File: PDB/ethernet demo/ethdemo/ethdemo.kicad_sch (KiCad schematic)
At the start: 102 parts, among them J1 0826-1X1T-GJ-F, J2 0826-1X1T-GJ-F, Q1 CSD19538Q3AT, U1 STM32H742VGTx, U2 KSZ8863RLLI, U3 TPS23861PWR, Y1 25MHz

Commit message: finished PoE schem start demo layout
started layout and fixed crystal footprint, still need to do I2C on MCU and RMII, need confirmation that MCU labels are old and can be overwritten
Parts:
- added R32: 10kOhm, Resistor_SMD:R_0603_1608Metric, symbol Device:R
- C24, C25: value 5pF -> 10pF
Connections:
- net +3.3V: now also C10.1, R47.2, U3.1 (VDD), U3.2 (~{RESET}), U3.24 (~{SHTDWN}), R32.2; no longer R48.2
- net Clock: now also U3.3 (SCL); no longer R31.2, U2.36 (SCL_MDC)
- net Data: now also U3.4 (SDAI), U3.5 (SDAO), R32.1
- net GND: now also R48.2; no longer R47.2, U3.23 (A3), U3.3 (SCL), U3.4 (SDAI)
- net P1LED0: no longer J1.19, R47.1
- net P1LED1: no longer J1.17, R48.1
- net P2LED0: now also J1.19, R47.1
- net P2LED1: now also J1.17, R48.1
- net Lost Connect: now reaches R30.1
- new net Address: U3.23 (A3)
- new net Cock: R31.2, U2.36 (SCL_MDC)
- no-connect marks 64 -> 63
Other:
- moved on the sheet: C10, C11, C12, C15, C16, C17, C18, C19, C20, C21, C22, C23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

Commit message: Finished first draft of demo schem
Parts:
- removed D1, D2: LED, LED_SMD:LED_0805_2012Metric, symbol Device:LED
- removed D6: 60V, symbol Device:D_Zener
- removed D7: 100V, symbol Device:D_Zener
- removed R1, R2: 270, Resistor_SMD:R_0603_1608Metric, symbol Device:R
- added D6: SMCJ60A, foot:SMCJ60A, symbol sym&foot:SMCJ60A
- added D7: SMAJ4764A-TP, foot:SMAJ100CA_13_F, symbol sym&foot:SMAJ4764A-TP
- C12, C15, C16, C17, C18, C19, C20, C21, C22, C23, C24, C25, C26, C27, C28, C29, C30, C31, C32, C33, C34, C35, C36: footprint (none) -> Capacitor_SMD:C_0603_1608Metric
- J1, J2: footprint 0826-1X1T-GJ-F:BEL_0826-1X1T-GJ-F -> foot:0826-1X1T-GJ-F
- R12, R13, R14, R15, R16, R17, R18, R19, R20, R21, R22, R23, R24, R25, R26, R27, R28, R29, R30, R31, R34, R35, R36, R37, R38, R39, R40, R41, R42, R43, R44, R45, R46, R47, R48, R49, R50: footprint (none) -> Resistor_SMD:R_0603_1608Metric
- U2: footprint LQFP-48_MCL -> foot:KSZ8863RLLI
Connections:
- net Cock is gone; now on net Clock: R31.2, U2.36 (SCL_MDC)
- net MOSI is gone; now on net CRS_DV: U1.31 (PA7)
- net PB11 is gone; now on net TX_EN: U1.47 (PB11)
- net PC4 is gone; now on net RXD0: U1.32 (PC4)
- net PC5 is gone; now on net RXD1: U1.33 (PC5)
- net UART4_RX is gone; now on net REF_CLK: U1.23 (PA1)
- net 48V: now also D6.1
- net Clock: now also U1.92 (PB6)
- net Data: now also U1.93 (PB7)
- net GND: now also D7.2
- net TXD0: now also U1.51 (PB12)
- net TXD1: now also U1.52 (PB13)
- net V-: now also D6.2, D7.1
- net OSC0: now reaches U1.12 (PH0)
- net OSC0: now also C25.1, Y1.2
- net OCS1: now reaches U1.13 (PH1)
- net OSC1: now reaches C24.2, Y1.1
- no-connect marks 63 -> 59
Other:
- note removed: "TBD"

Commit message: Started demo layout
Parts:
- removed R30: Interupt, Resistor_SMD:R_0603_1608Metric, symbol Device:R_Small
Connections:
- net +3.3V: now also R47.1; no longer R47.2
- net Lost Connect: now also R35.2, U2.35 (INTRN)
- net P2LED0: now also R47.2; no longer R47.1
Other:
- moved on the sheet: R47
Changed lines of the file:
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@@
 	)
 	(junction
-		(at 497.84 246.38)
-		(diameter 0)
-		(color 0 0 0 0)
-	)
-	(junction
 		(at 402.59 204.47)
 		(diameter 0)
@@
 	(wire
 		(pts
-			(xy 436.88 218.44) (xy 453.39 218.44)
-		)
-		(stroke
-			(width 0)
-			(type default)
-		)
-	)
-	(wire
-		(pts
 			(xy 298.45 81.28) (xy 302.26 81.28)
 		)
@@
 	(wire
 		(pts
-			(xy 417.83 218.44) (xy 431.8 218.44)
+			(xy 417.83 218.44) (xy 453.39 218.44)
 		)
 		(stroke
@@
 	(wire
 		(pts
-			(xy 497.84 245.11) (xy 497.84 246.38)
-		)
-		(stroke
-			(width 0)
-			(type default)
-		)
-	)
-	(wire
-		(pts
 			(xy 328.93 199.39) (xy 337.82 199.39)
 		)
@@
 	(wire
 		(pts
+			(xy 497.84 246.38) (xy 497.84 247.65)
+		)
+		(stroke
+			(width 0)
+			(type default)
+		)
+	)
+	(wire
+		(pts
 			(xy 396.24 266.7) (xy 396.24 276.86)
 		)
@@
 	(wire
 		(pts
-			(xy 497.84 246.38) (xy 497.84 247.65)
-		)
-		(stroke
-			(width 0)
-			(type default)
-		)
-	)
-	(wire
-		(pts
 			(xy 495.3 284.48) (xy 504.19 284.48)
 		)
@@
 	(symbol
 		(lib_id "Device:R_Small")
-		(at 492.76 297.18 270)
+		(at 492.76 297.18 90)
 		(unit 1)
 		(body_style 1)
@@
 		(dnp no)
 		(property "Reference" "R47"
-			(at 492.76 295.656 90)
+			(at 492.76 298.704 90)
 			(show_name no)
 			(do_not_autoplace no)
@@
 		)
 		(property "Value" "1kOhm"
-			(at 492.76 298.958 90)
+			(at 492.76 295.402 90)
 			(show_name no)
 			(do_not_autoplace no)
@@
 					(unit 1)
 				)
-			)
-		)
-	)
-	(symbol
-		(lib_id "Device:R_Small")
-		(at 434.34 218.44 270)
-		(unit 1)
-		(body_style 1)
-		(exclude_from_sim no)
-		(in_bom yes)
-		(on_board yes)
-		(in_pos_files yes)
-		(dnp no)
-		(property "Reference" "R30"
-			(at 434.34 214.884 90)
-			(show_name no)
-			(do_not_autoplace no)
-			(effects
-				(font
-					(size 1.016 1.016)
-				)
-			)
-		)
-		(property "Value" "Interupt"
-			(at 434.34 216.662 90)
-			(show_name no)
-			(do_not_autoplace no)
-			(effects
-				(font
-					(size 1.27 1.27)
-				)
-			)
-		)
-		(property "Footprint" "Resistor_SMD:R_0603_1608Metric"
-			(at 434.34 218.44 0)
-			(hide yes)
-			(show_name no)
-			(do_not_autoplace no)
-			(effects
-				(font
-					(size 1.27 1.27)
-				)
-			)
-		)
-		(property "Datasheet" ""
-			(at 434.34 218.44 0)
-			(hide yes)
-			(show_name no)
-			(do_not_autoplace no)
-			(effects
-				(font
-					(size 1.27 1.27)
-				)
-			)
-		)
-		(property "Description" "Active low to MCU to express lost link"
-			(at 434.34 218.44 0)
-			(hide yes)
-			(show_name no)
-			(do_not_autoplace no)
-			(effects
-				(font
-					(size 1.27 1.27)
-				)
-			)
-		)
-		(pin "2"
-		)
-		(pin "1"
-		)
-		(instances
-			(project "ethdemo"
-				(path "/7dabef91-f4a1-42f5-98eb-8cd98e55ead9"
-					(reference "R30")
-					(unit 1)
-				)

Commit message: worked on eth ic routing
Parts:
- D8: footprint Diode_THT:D_DO-41_SOD81_P10.16mm_Horizontal -> Diode_SMD:D_SMA
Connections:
- net TX2-: now reaches J1.10 (TRD1-), R18.1, U2.11 (TXM2)
- net TX2+: now reaches J1.11 (TRD1+), R17.1, U2.12 (TXP2)
- net RX2+: now reaches J1.4 (TRD2+), R19.2, U2.9 (RXP2)
- net RX2-: now reaches J1.5 (TRD2-), R20.2, U2.8 (RXM2)
- net D2+: now reaches J2.4 (TRD2+), R15.2, U2.2 (RXP1)
- net D1+: now reaches J2.11 (TRD1+), R12.1, U2.4 (TXP1)
- net D1-: now reaches J2.10 (TRD1-), R13.1, U2.3 (TXM1)
- net D2-: now reaches J2.5 (TRD2-), R14.2, U2.1 (RXM1)
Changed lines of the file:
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@@
 		)
 	)
+	(label "D1-"
+		(at 414.02 276.86 0)
+		(effects
+			(font
+				(size 1.27 1.27)
+			)
+			(justify left bottom)
+		)
+	)
 	(label "P2LED1"
 		(at 394.97 195.58 180)
@@
 		)
 	)
+	(label "D2-"
+		(at 419.1 289.56 0)
+		(effects
+			(font
+				(size 1.27 1.27)
+			)
+			(justify left bottom)
+		)
+	)
 	(label "P2LED0"
 		(at 394.97 193.04 180)
@@
 		)
 	)
+	(label "TX2+"
+		(at 391.16 251.46 0)
+		(effects
+			(font
+				(size 1.27 1.27)
+			)
+			(justify left bottom)
+		)
+	)
 	(label "PA3"
 		(at 64.77 52.07 90)
@@
 		)
 	)
+	(label "RX2+"
+		(at 391.16 256.54 0)
+		(effects
+			(font
+				(size 1.27 1.27)
+			)
+			(justify left bottom)
+		)
+	)
 	(label "D-"
 		(at 85.09 52.07 90)
@@
 		)
 	)
+	(label "D2+"
+		(at 419.1 284.48 0)
+		(effects
+			(font
+				(size 1.27 1.27)
+			)
+			(justify left bottom)
+		)
+	)
 	(label "PC12"
 		(at 173.99 52.07 90)
@@
 		)
 	)
+	(label "TX2-"
+		(at 391.16 254 0)
+		(effects
+			(font
+				(size 1.27 1.27)
+			)
+			(justify left bottom)
+		)
+	)
 	(label "Data"
 		(at 30.48 365.76 0)
@@
 		)
 	)
+	(label "RX2-"
+		(at 391.16 259.08 0)
+		(effects
+			(font
+				(size 1.27 1.27)
+			)
+			(justify left bottom)
+		)
+	)
 	(label "RXD1"
 		(at 156.21 52.07 90)
@@
 		)
 	)
+	(label "D1+"
+		(at 412.75 274.32 0)
+		(effects
+			(font
+				(size 1.27 1.27)
+			)
+			(justify left bottom)
+		)
+	)
 	(symbol
 		(lib_id "power:+3.3V")
@@
 			)
 		)
-		(property "Footprint" "Diode_THT:D_DO-41_SOD81_P10.16mm_Horizontal"
+		(property "Footprint" "Diode_SMD:D_SMA"
 			(at 323.85 232.41 0)
 			(hide yes)
@@
 			)
 		)
-		(property "Description" "50V 1A General Purpose Rectifier Diode, DO-41"
+		(property "Description" "DIODE STANDARD 1000V 1A DO214AC"
 			(at 323.85 232.41 0)
 			(hide yes)

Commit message: mostly finished routing and board design
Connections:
- net RXD0 renamed RX-
- net RXD1 renamed RX+
- net TXD0 renamed TX-
- net TXD1 renamed TX+
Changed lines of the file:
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@@
+		)
+	)
+	(label "RX+"
+		(at 321.31 213.36 180)
+		(effects
+			(font
+				(size 1.27 1.27)
+			)
+			(justify right bottom)
 		)
 	)
@@
 		)
 	)
+	(label "RX-"
+		(at 321.31 215.9 180)
+		(effects
+			(font
+				(size 1.27 1.27)
+			)
+			(justify right bottom)
+		)
+	)
 	(label "P2LED0"
 		(at 394.97 193.04 180)
@@
 		)
 	)
-	(label "TXD1"
-		(at 133.35 52.07 90)
-		(effects
-			(font
-				(size 1.27 1.27)
-			)
-			(justify left bottom)
-		)
-	)
 	(label "Clock"
 		(at 115.57 52.07 90)
@@
 		)
 	)
-	(label "TXD1"
+	(label "TX+"
 		(at 440.69 236.22 180)
 		(effects
@@
 		)
 	)
+	(label "TX+"
+		(at 133.35 52.07 90)
+		(effects
+			(font
+				(size 1.27 1.27)
+			)
+			(justify left bottom)
+		)
+	)
 	(label "PA3"
 		(at 64.77 52.07 90)
@@
 		)
 	)
-	(label "TXD0"
+	(label "TX-"
 		(at 440.69 233.68 180)
 		(effects
@@
 		)
 	)
-	(label "TXD0"
+	(label "TX-"
 		(at 130.81 52.07 90)
 		(effects
@@
 		)
 	)
-	(label "RXD0"
+	(label "RX-"
 		(at 153.67 52.07 90)
 		(effects
@@
 		)
 	)
-	(label "RXD0"
-		(at 321.31 215.9 0)
-		(effects
-			(font
-				(size 1.27 1.27)
-			)
-			(justify left bottom)
-		)
-	)
 	(label "TX_EN"
 		(at 447.04 243.84 180)
@@
 		)
 	)
-	(label "RXD1"
-		(at 321.31 213.36 0)
-		(effects
-			(font
-				(size 1.27 1.27)
-			)
-			(justify left bottom)
-		)
-	)
 	(label "TX2-"
 		(at 391.16 254 0)
@@
 		)
 	)
-	(label "RXD1"
+	(label "RX+"
 		(at 156.21 52.07 90)
 		(effects

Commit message: Fixed crystal footprint
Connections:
- net GND: now also Y1.2 (GND)
- net OSC0: now also Y1.1; no longer Y1.2
- net OSC1: now also Y1.3 (2); no longer Y1.1
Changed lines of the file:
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@@
 	(wire
 		(pts
+			(xy 306.07 88.9) (xy 306.07 86.36)
+		)
+		(stroke
+			(width 0)
+			(type default)
+		)
+	)
+	(wire
+		(pts
 			(xy 494.03 256.54) (xy 473.71 256.54)
 		)
@@
 	(wire
 		(pts
+			(xy 309.88 81.28) (xy 313.69 81.28)
+		)
+		(stroke
+			(width 0)
+			(type default)
+		)
+	)
+	(wire
+		(pts
 			(xy 71.12 378.46) (xy 88.9 378.46)
 		)
@@
 	(wire
 		(pts
-			(xy 313.69 81.28) (xy 309.88 81.28)
-		)
-		(stroke
-			(width 0)
-			(type default)
-		)
-	)
-	(wire
-		(pts
 			(xy 314.96 217.17) (xy 323.85 217.17)
 		)
@@
 	)
 	(symbol
+		(lib_id "power:GND")
+		(at 306.07 88.9 0)
+		(unit 1)
+		(body_style 1)
+		(exclude_from_sim no)
+		(in_bom yes)
+		(on_board yes)
+		(in_pos_files yes)
+		(dnp no)
+		(fields_autoplaced yes)
+		(property "Reference" "#PWR01"
+			(at 306.07 95.25 0)
+			(hide yes)
+			(show_name no)
+			(do_not_autoplace no)
+			(effects
+				(font
+					(size 1.27 1.27)
+				)
+			)
+		)
+		(property "Value" "GND"
+			(at 306.07 93.98 0)
+			(show_name no)
+			(do_not_autoplace no)
+			(effects
+				(font
+					(size 1.27 1.27)
+				)
+			)
+		)
+		(property "Footprint" ""
+			(at 306.07 88.9 0)
+			(hide yes)
+			(show_name no)
+			(do_not_autoplace no)
+			(effects
+				(font
+					(size 1.27 1.27)
+				)
+			)
+		)
+		(property "Datasheet" ""
+			(at 306.07 88.9 0)
+			(hide yes)
+			(show_name no)
+			(do_not_autoplace no)
+			(effects
+				(font
+					(size 1.27 1.27)
+				)
+			)
+		)
+		(property "Description" "Power symbol creates a global label with name \"GND\" , ground"
+			(at 306.07 88.9 0)
+			(hide yes)
+			(show_name no)
+			(do_not_autoplace no)
+			(effects
+				(font
+					(size 1.27 1.27)
+				)
+			)
+		)
+		(pin "1"
+		)
+		(instances
+			(project "ethdemo"
+				(path "/7dabef91-f4a1-42f5-98eb-8cd98e55ead9"
+					(reference "#PWR01")
+					(unit 1)
+				)
+			)
+		)
+	)
+	(symbol
 		(lib_id "Device:R_Small")
 		(at 402.59 293.37 0)
@@
 	(symbol
 		(lib_id "Device:Crystal")
-		(at 306.07 81.28 180)
+		(at 306.07 81.28 0)
 		(unit 1)
 		(body_style 1)
@@
 		(dnp no)
 		(property "Reference" "Y1"
-			(at 309.372 79.248 0)
+			(at 302.768 83.312 0)
 			(show_name no)
 			(do_not_autoplace no)
@@
 		)
 		(property "Value" "25MHz"
-			(at 306.07 85.598 0)
+			(at 306.07 76.962 0)
 			(show_name no)
 			(do_not_autoplace no)
@@
 			)
 		)
-		(pin "2"
+		(pin "3"
 		)
 		(pin "1"
 		)
+		(pin "2"
+		)
 		(instances

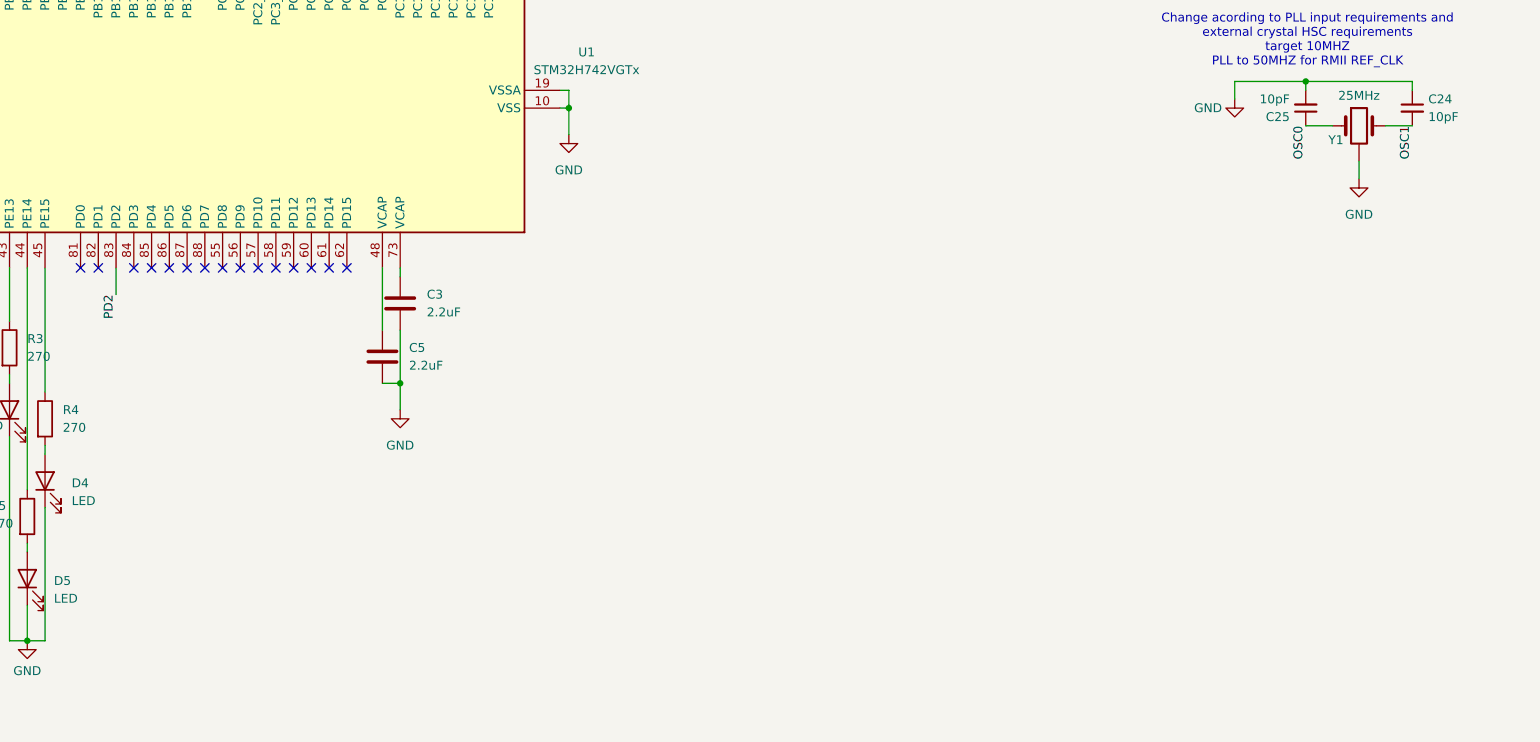
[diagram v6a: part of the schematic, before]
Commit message: did impedance and length tuning and control
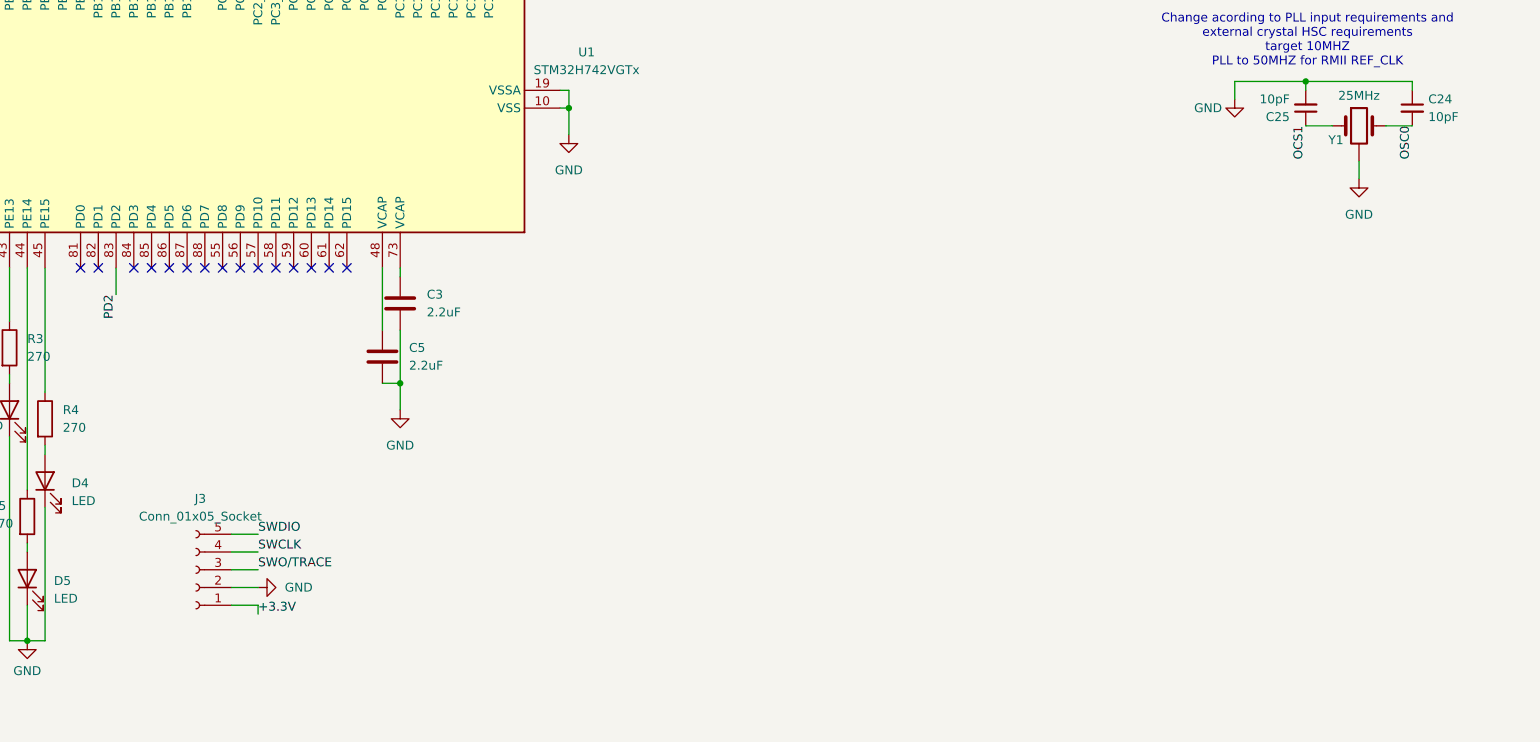
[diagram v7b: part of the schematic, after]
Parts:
- added J3: Conn_01x05_Socket, Connector_PinSocket_2.54mm:PinSocket_1x05_P2.54mm_Vertical, symbol Connector:Conn_01x05_Socket
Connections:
- net OSC1 is gone; now on net OSC0: C24.2, Y1.3 (2)
- net +3.3V: now also J3.1 (Pin_1)
- net GND: now also J3.2 (Pin_2)
- net OCS1: now also C25.1, Y1.1
- net OSC0: no longer C25.1, Y1.1
- net SWCLK: now also J3.4 (Pin_4)
- net SWDIO: now also J3.5 (Pin_5)
- net SWO/TRACE: now also J3.3 (Pin_3)

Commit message: found a USBC jack
added symbol to schem and linked footprint but not in layout yet
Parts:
- added J4: 2171790001, 2171790001_MOL, symbol sym&foot:2171790001
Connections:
- net D+: now also J4.A6 (DP1)
- net D-: now also J4.A7 (DN1)
- net GND: now also J4.A1/B12 (GND), J4.B1/A12 (GND)
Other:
- note added: "Magnetics internal to magjacks"
- note removed: "Magnetics and Bob Smith termination internal to magjacks"
